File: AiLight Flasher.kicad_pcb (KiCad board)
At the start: 2 copper layers, 30 x 30 mm, 9 parts, among them J1 GND, J2 IO0, J3 3V3, J4 aRX, J5 aTX, J6 FTDI

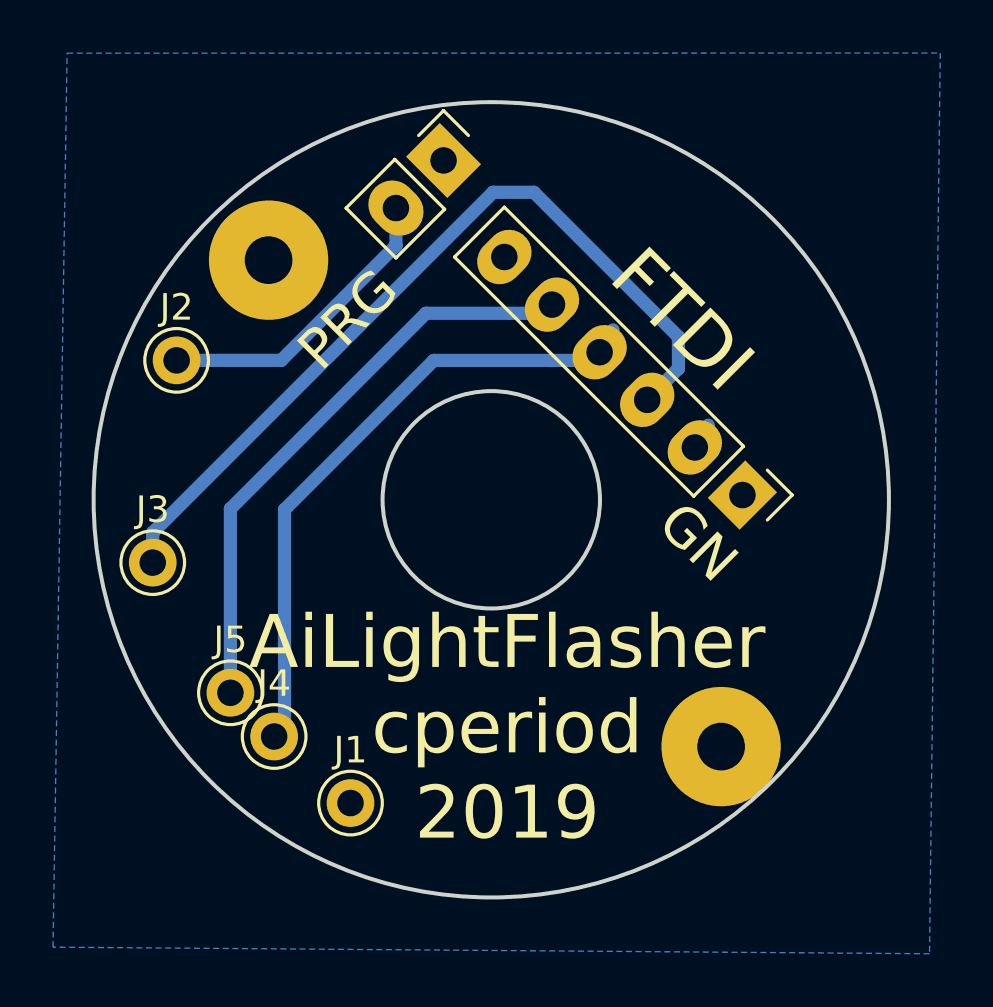
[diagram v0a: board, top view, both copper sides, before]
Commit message: more position tweaks
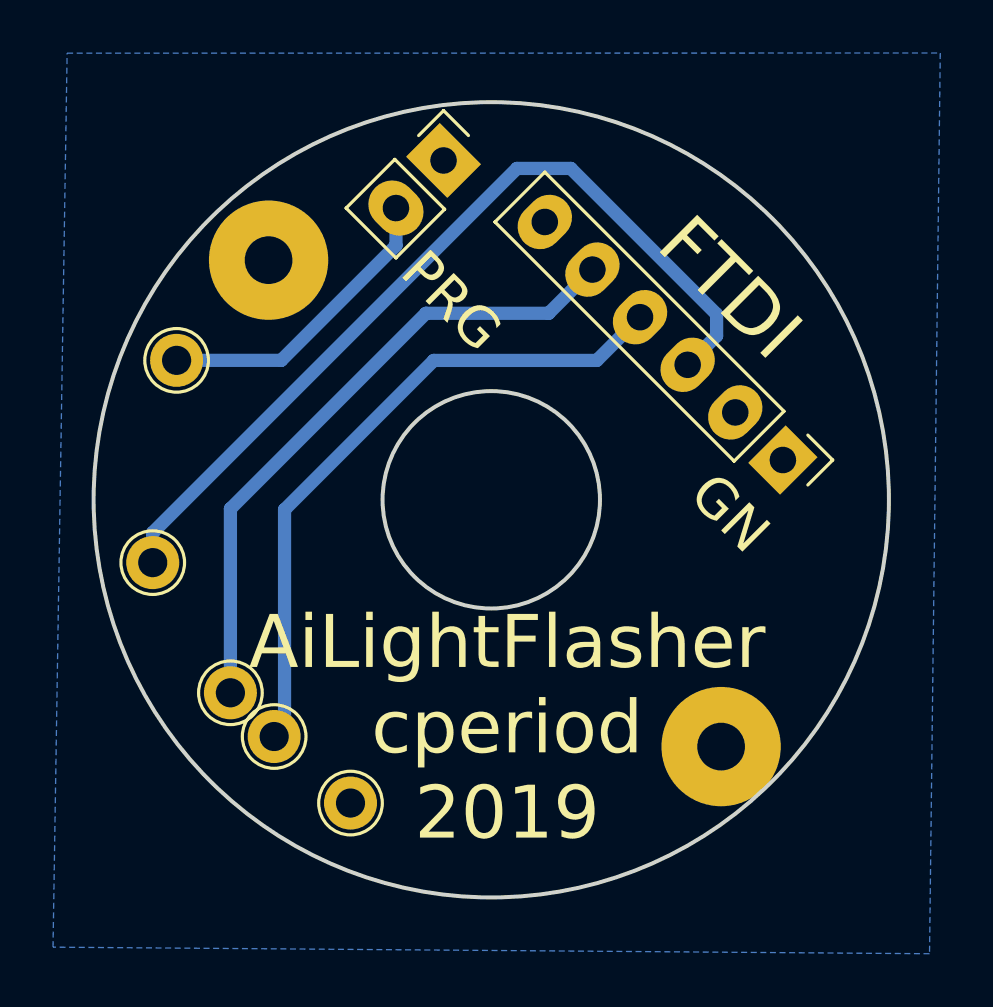
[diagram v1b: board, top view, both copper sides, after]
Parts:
- J1, J2, J3, J4, J5: footprint CPB:Test_Point_THTPad_d2.0mm_Drill1.0mm -> CPB:Test_Point_THTPad_d2.0mm_Drill1.1mm
- moved J6 2.02 mm to (111.0, 98.5)
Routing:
- net aTX: track 22.3 -> 24.3 mm
- net 3V3: track 31.4 -> 32.7 mm
- net aRX: track 24.2 -> 25.1 mm

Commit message: move the FTDI header back out a bit, tweak labels, etc
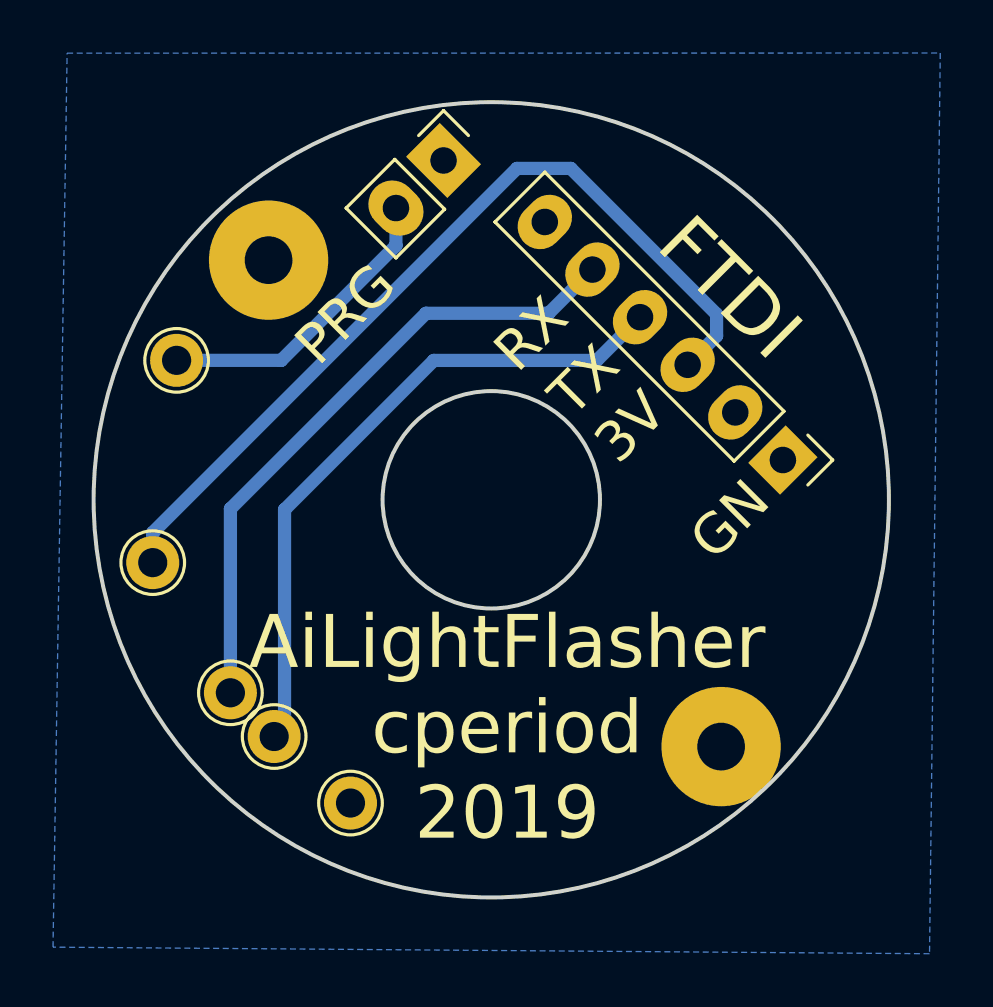
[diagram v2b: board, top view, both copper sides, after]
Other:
- board text added: "3V"
- board text added: "RX"
- board text added: "TX"
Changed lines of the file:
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@@
   (general
     (thickness 1.6)
-    (drawings 6)
+    (drawings 9)
     (tracks 19)
     (zones 0)
@@
   )
   (setup
-    (last_trace_width 0.5)
+    (last_trace_width 0.25)
     (user_trace_width 0.5)
     (trace_clearance 0.2)
@@
       (effects (font (size 1 1) (thickness 0.15)))
     )
-    (fp_text value Jumper (at 0 4.87 315) (layer F.Fab)
+    (fp_text value Jumper (at -2.934493 1.237437 45) (layer F.Fab)
       (effects (font (size 1 1) (thickness 0.15)))
     )
@@
       (net 5 aTX))
   )
+  (gr_text 3V (at 105.25 97.25 45) (layer F.SilkS)
+    (effects (font (size 1.5 1.5) (thickness 0.3)))
+  )
+  (gr_text TX (at 103.5 95.5 45) (layer F.SilkS)
+    (effects (font (size 1.5 1.5) (thickness 0.3)))
+  )
+  (gr_text RX (at 101.5 93.75 45) (layer F.SilkS)
+    (effects (font (size 1.5 1.5) (thickness 0.3)))
+  )
   (gr_circle (center 100 100) (end 104.1 100) (layer Edge.Cuts) (width 0.15))
-  (gr_text PRG (at 98.5 92.5 315) (layer F.SilkS)
+  (gr_text PRG (at 94.5 93 45) (layer F.SilkS)
     (effects (font (size 1.5 1.5) (thickness 0.3)))
   )
@@
     (effects (font (size 2 2) (thickness 0.3)))
   )
-  (gr_text GN (at 109 100.5 315) (layer F.SilkS)
-    (effects (font (size 1.5 1.5) (thickness 0.3)))
-  )
+  (gr_text GN (at 109 100.75 45) (layer F.SilkS)
+    (effects (font (size 1.5 1.5) (thickness 0.3)))
+  )
